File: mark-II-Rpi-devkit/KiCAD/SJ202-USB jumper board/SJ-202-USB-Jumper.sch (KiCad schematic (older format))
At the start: 3 parts, among them J1 USB_A, J2 USB3150-30-130-A, J3 Conn_01x05

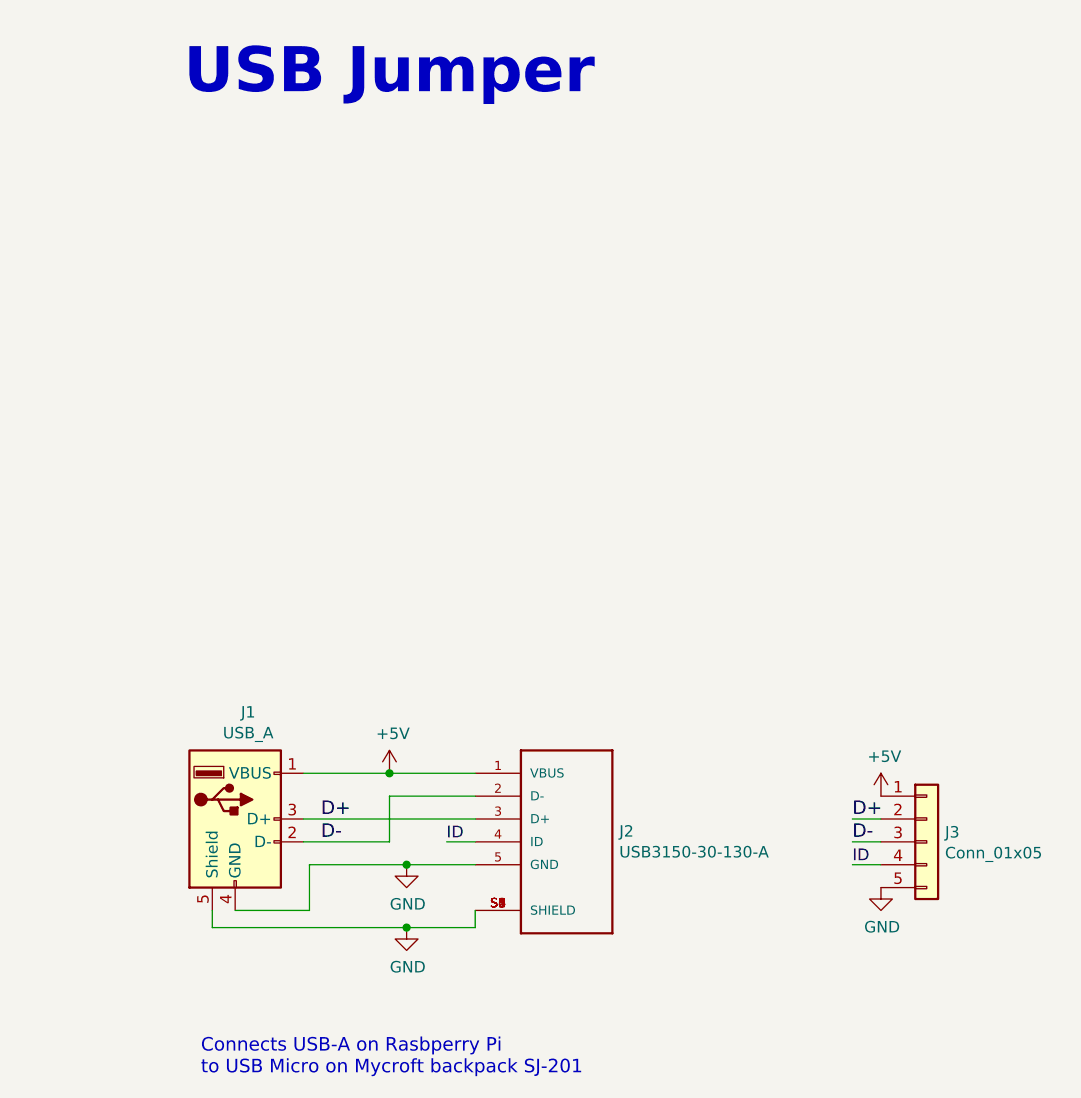
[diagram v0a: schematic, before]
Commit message: SJ201 - Removed CM108b soundcard, added in I2S to Line out, ATTin402. Moved holes in layout. SJ202 - extened length to plug into USB2.0 port
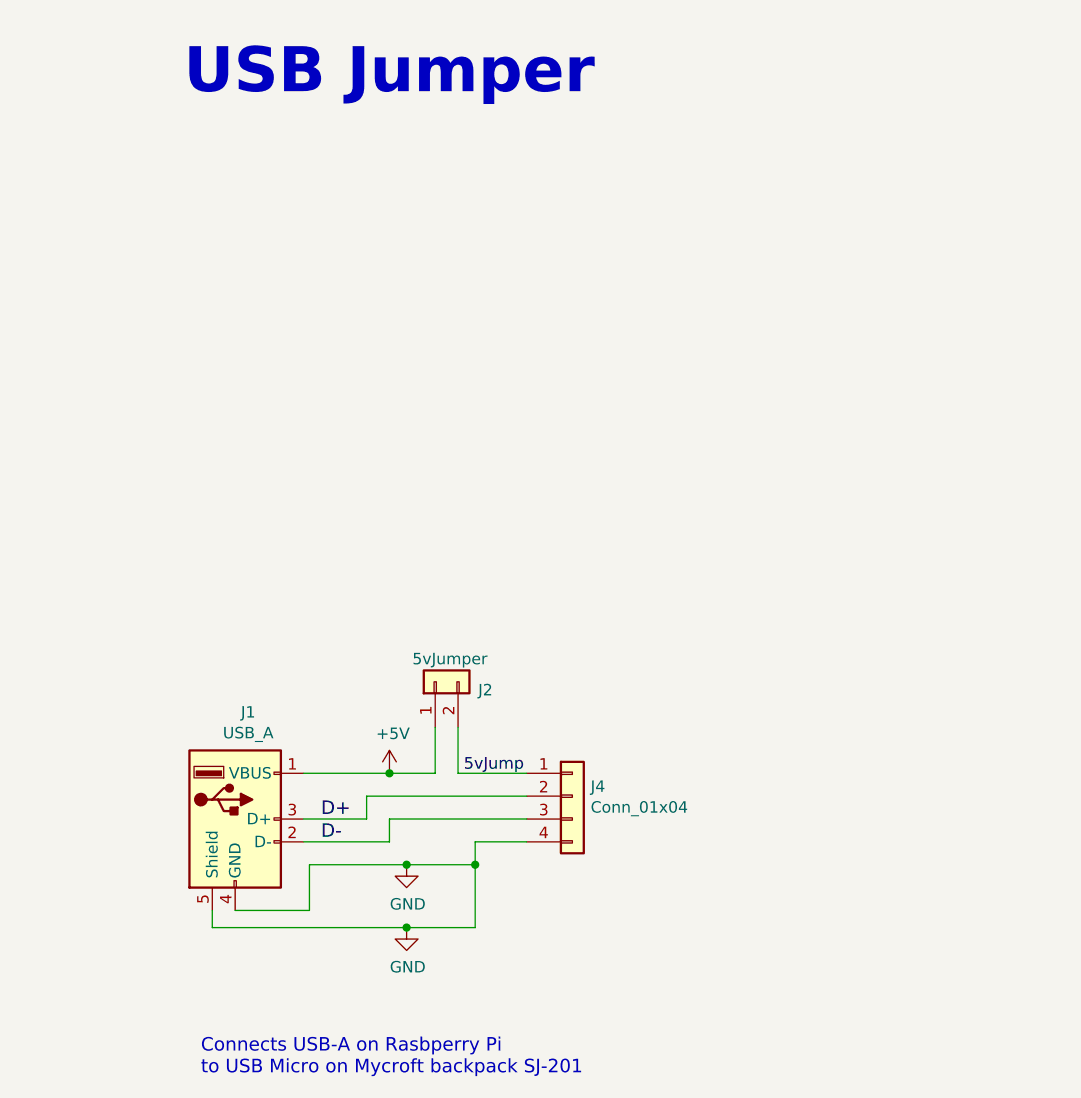
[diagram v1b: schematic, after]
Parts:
- removed J2: USB3150-30-130-A, GCT_USB3150-30-130-A, symbol USB3150-30-130-A:USB3150-30-130-A
- removed J3: Conn_01x05, Connector_PinHeader_2.54mm:PinHeader_1x05_P2.54mm_Vertical, symbol Connector_Generic:Conn_01x05
- added J2: 5vJumper, Jumper:SolderJumper-2_P1.3mm_Open_TrianglePad1.0x1.5mm, symbol Connector_Generic:Conn_01x02
- added J4: Conn_01x04, Connector_PinHeader_2.54mm:PinHeader_1x04_P2.54mm_Vertical, symbol Connector_Generic:Conn_01x04
- J1: Link (none) -> https://www.digikey.com/product-detail/en/0480372200/WM3983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; MPN (none) -> 0480372200
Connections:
- net +5V: now also J2.1 (Pin_1)
- net D+: now also J4.2 (Pin_2)
- net D-: now also J4.3 (Pin_3)
- net GND: now also J4.4 (Pin_4)
- new net 5vJump: J2.2 (Pin_2), J4.1 (Pin_1)
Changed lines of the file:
@@
 Sheet 1 1
 Title "SJ-202-USB-Jumper"
-Date "2020-09-04"
-Rev "01"
+Date "2020-09-27"
+Rev "02"
 Comp "Mycroft AI"
 Comment1 "SJ-202-01"
@@
 Comment4 ""
 $EndDescr
-$Comp
-L USB3150-30-130-A:USB3150-30-130-A J2
-U 1 1 5F5281B3
-P 5600 4175
-F 0 "J2" H 5830 4221 50  0000 L CNN
-F 1 "USB3150-30-130-A" H 5830 4130 50  0000 L CNN
-F 2 "GCT_USB3150-30-130-A" H 5600 4175 50  0001 L BNN
-F 3 "https://gct.co/files/drawings/usb3150.pdf" H 5600 4175 50  0001 L BNN
-F 4 "7.23mm" H 5600 4175 50  0001 L BNN "Field4"
-F 5 "A2" H 5600 4175 50  0001 L BNN "Field5"
-F 6 "GCT" H 5600 4175 50  0001 L BNN "Field6"
-F 7 "2073-USB3150-30-130-ACT-ND" H 5600 4175 50  0001 C CNN "Digikey"
-	1    5600 4175
-	1    0    0    -1
-$EndComp
 $Comp
 L Connector:USB_A J1
@@
 F 3 "https://www.digikey.com/product-detail/en/0480372200/WM3983CT-ND/2421836" H 4300 4025 50  0001 C CNN
 F 4 "WM3983CT-ND" H 4150 4075 50  0001 C CNN "Digikey"
+F 5 "0480372200" H 4150 4075 50  0001 C CNN "MPN"
+F 6 "https://www.digikey.com/product-detail/en/0480372200/WM3983CT-ND/2421836" H 4150 4075 50  0001 C CNN "Link"
 	1    4150 4075
 	1    0    0    -1
 $EndComp
-Wire Wire Line
-	5200 3875 4825 3875
-Wire Wire Line
-	4450 4075 5200 4075
-Wire Wire Line
-	5200 3975 4825 3975
-Wire Wire Line
-	4825 3975 4825 4175
 Wire Wire Line
 	4825 4175 4450 4175
@@
 Wire Wire Line
 	4050 4475 4050 4550
-Wire Wire Line
-	5200 4550 5200 4475
 $Comp
 L power:GND #PWR0101
@@
 	1    0    0    -1
 $EndComp
-Connection ~ 4825 3875
 Wire Wire Line
 	4825 3875 4450 3875
@@
 Text Notes 4000 5200 0    59   ~ 0
 Connects USB-A on Rasbperry Pi\nto USB Micro on Mycroft backpack SJ-201
-$Comp
-L Connector_Generic:Conn_01x05 J3
-U 1 1 5F52F406
-P 7175 4175
-F 0 "J3" H 7255 4217 50  0000 L CNN
-F 1 "Conn_01x05" H 7255 4126 50  0000 L CNN
-F 2 "Connector_PinHeader_2.54mm:PinHeader_1x05_P2.54mm_Vertical" H 7175 4175 50  0001 C CNN
-F 3 "~" H 7175 4175 50  0001 C CNN
-	1    7175 4175
-	1    0    0    -1
-$EndComp
 Wire Wire Line
 	4475 4475 4150 4475
@@
 Wire Wire Line
 	4900 4275 4475 4275
-$Comp
-L power:GND #PWR0104
-U 1 1 5F5305F9
-P 6975 4375
-F 0 "#PWR0104" H 6975 4125 50  0001 C CNN
-F 1 "GND" H 6980 4202 50  0000 C CNN
-F 2 "" H 6975 4375 50  0001 C CNN
-F 3 "" H 6975 4375 50  0001 C CNN
-	1    6975 4375
-	1    0    0    -1
-$EndComp
 Text Label 4525 4175 0    59   ~ 0
 D-
 Text Label 4525 4075 0    59   ~ 0
 D+
-Text Label 6850 4075 0    59   ~ 0
-D+
-Text Label 6850 4175 0    59   ~ 0
-D-
 $Comp
-L power:+5V #PWR0105
-U 1 1 5F530B0F
-P 6975 3975
-F 0 "#PWR0105" H 6975 3825 50  0001 C CNN
-F 1 "+5V" H 6990 4148 50  0000 C CNN
-F 2 "" H 6975 3975 50  0001 C CNN
-F 3 "" H 6975 3975 50  0001 C CNN
-	1    6975 3975
+L Connector_Generic:Conn_01x04 J4
+U 1 1 5F58F2C6
+P 5625 3975
+F 0 "J4" H 5705 4017 50  0000 L CNN
+F 1 "Conn_01x04" H 5705 3926 50  0000 L CNN
+F 2 "Connector_PinHeader_2.54mm:PinHeader_1x04_P2.54mm_Vertical" H 5625 3975 50  0001 C CNN
+F 3 "~" H 5625 3975 50  0001 C CNN
+F 4 "C124378" H 5625 3975 50  0001 C CNN "MPN"
+F 5 "C124378" H 5625 3975 50  0001 C CNN "LCSC"
+F 6 "https://lcsc.com/product-detail/Pin-Header-Female-Header_Ckmtw-Shenzhen-Cankemeng-C124378_C124378.html" H 5625 3975 50  0001 C CNN "Link"
+	1    5625 3975
 	1    0    0    -1
 $EndComp
+$Comp
+L Connector_Generic:Conn_01x02 J2
+U 1 1 5F596E74
+P 5025 3475
+F 0 "J2" V 4989 3287 50  0000 R CNN
+F 1 "5vJumper" V 5125 3575 50  0000 R CNN
+F 2 "Jumper:SolderJumper-2_P1.3mm_Open_TrianglePad1.0x1.5mm" H 5025 3475 50  0001 C CNN
+F 3 "~" H 5025 3475 50  0001 C CNN
+F 4 "DNP" H 5025 3475 50  0001 C CNN "MPN"
+	1    5025 3475
+	0    -1   -1   0
+$EndComp
 Wire Wire Line
-	6975 4075 6850 4075
+	5025 3675 5025 3875
 Wire Wire Line
-	6975 4175 6850 4175
+	5025 3875 4825 3875
+Connection ~ 4825 3875
 Wire Wire Line
-	5075 4175 5200 4175
-Text Label 5075 4175 0    51   ~ 0
-ID
-Text Label 6850 4275 0    51   ~ 0
-ID
+	5125 3675 5125 3875
+Connection ~ 5200 4275
 Wire Wire Line
-	6975 4275 6850 4275
+	5200 4275 5200 4550
+Wire Wire Line
+	5200 4175 5200 4275
+Wire Wire Line
+	4825 4075 4825 4175
+Wire Wire Line
+	4725 3975 4725 4075
+Wire Wire Line
+	4725 4075 4450 4075
+Text Label 5150 3875 0    51   ~ 0
+5vJump
+Wire Wire Line
+	5125 3875 5425 3875
+Wire Wire Line
+	4725 3975 5425 3975
+Wire Wire Line
+	4825 4075 5425 4075
+Wire Wire Line
+	5200 4175 5425 4175
 $EndSCHEMATC

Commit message: SJ-201 v3, sent to PCB Fab. Removed USB Hub, add in I2S to Line Out
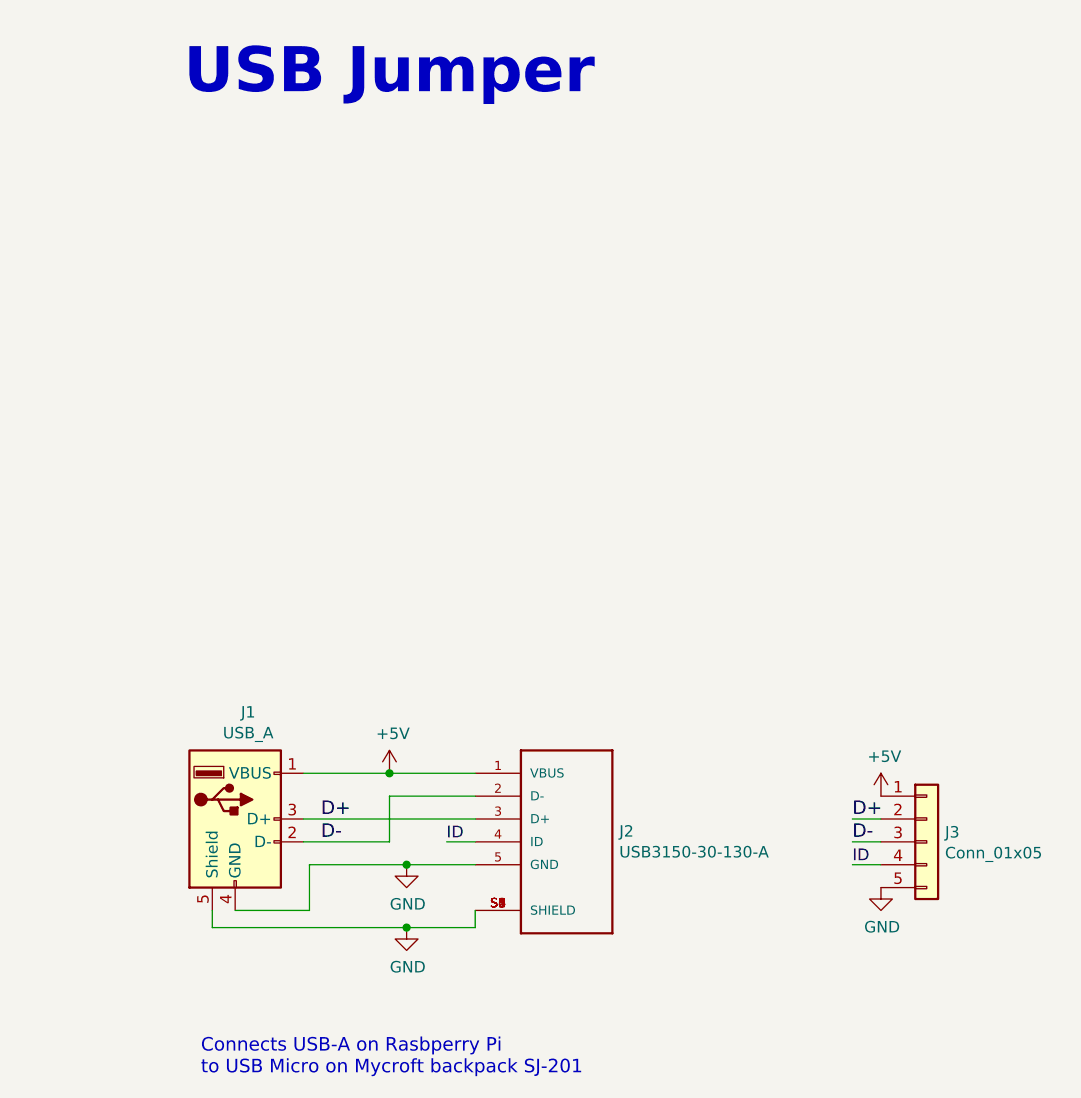
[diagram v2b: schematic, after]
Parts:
- removed J2: 5vJumper, Jumper:SolderJumper-2_P1.3mm_Open_TrianglePad1.0x1.5mm, symbol Connector_Generic:Conn_01x02
- removed J4: Conn_01x04, Connector_PinHeader_2.54mm:PinHeader_1x04_P2.54mm_Vertical, symbol Connector_Generic:Conn_01x04
- added J2: USB3150-30-130-A, GCT_USB3150-30-130-A, symbol USB3150-30-130-A:USB3150-30-130-A
- added J3: Conn_01x05, Connector_PinHeader_2.54mm:PinHeader_1x05_P2.54mm_Vertical, symbol Connector_Generic:Conn_01x05
- J1: Link https://www.digikey.com/product-detail/en/0480372200/WM3983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 -> (none); MPN 0480372200 -> (none)
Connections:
- net +5V: now also J2.1 (VBUS), J3.1 (Pin_1)
- net D+: now also J2.3 (D+), J3.2 (Pin_2)
- net D-: now also J2.2 (D-), J3.3 (Pin_3)
- net GND: now also J2.5 (GND), J2.S1 (SHIELD), J2.S2 (SHIELD), J2.S3 (SHIELD), J2.S4 (SHIELD), J2.S5 (SHIELD), J2.S6 (SHIELD), J3.5 (Pin_5)
- new net ID: J2.4 (ID), J3.4 (Pin_4)
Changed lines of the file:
@@
 Sheet 1 1
 Title "SJ-202-USB-Jumper"
-Date "2020-09-27"
-Rev "02"
+Date "2020-09-04"
+Rev "01"
 Comp "Mycroft AI"
 Comment1 "SJ-202-01"
@@
 Comment4 ""
 $EndDescr
+$Comp
+L USB3150-30-130-A:USB3150-30-130-A J2
+U 1 1 5F5281B3
+P 5600 4175
+F 0 "J2" H 5830 4221 50  0000 L CNN
+F 1 "USB3150-30-130-A" H 5830 4130 50  0000 L CNN
+F 2 "GCT_USB3150-30-130-A" H 5600 4175 50  0001 L BNN
+F 3 "https://gct.co/files/drawings/usb3150.pdf" H 5600 4175 50  0001 L BNN
+F 4 "7.23mm" H 5600 4175 50  0001 L BNN "Field4"
+F 5 "A2" H 5600 4175 50  0001 L BNN "Field5"
+F 6 "GCT" H 5600 4175 50  0001 L BNN "Field6"
+F 7 "2073-USB3150-30-130-ACT-ND" H 5600 4175 50  0001 C CNN "Digikey"
+	1    5600 4175
+	1    0    0    -1
+$EndComp
 $Comp
 L Connector:USB_A J1
@@
 F 3 "https://www.digikey.com/product-detail/en/0480372200/WM3983CT-ND/2421836" H 4300 4025 50  0001 C CNN
 F 4 "WM3983CT-ND" H 4150 4075 50  0001 C CNN "Digikey"
-F 5 "0480372200" H 4150 4075 50  0001 C CNN "MPN"
-F 6 "https://www.digikey.com/product-detail/en/0480372200/WM3983CT-ND/2421836" H 4150 4075 50  0001 C CNN "Link"
 	1    4150 4075
 	1    0    0    -1
 $EndComp
+Wire Wire Line
+	5200 3875 4825 3875
+Wire Wire Line
+	4450 4075 5200 4075
+Wire Wire Line
+	5200 3975 4825 3975
+Wire Wire Line
+	4825 3975 4825 4175
 Wire Wire Line
 	4825 4175 4450 4175
@@
 Wire Wire Line
 	4050 4475 4050 4550
+Wire Wire Line
+	5200 4550 5200 4475
 $Comp
 L power:GND #PWR0101
@@
 	1    0    0    -1
 $EndComp
+Connection ~ 4825 3875
 Wire Wire Line
 	4825 3875 4450 3875
@@
 Text Notes 4000 5200 0    59   ~ 0
 Connects USB-A on Rasbperry Pi\nto USB Micro on Mycroft backpack SJ-201
+$Comp
+L Connector_Generic:Conn_01x05 J3
+U 1 1 5F52F406
+P 7175 4175
+F 0 "J3" H 7255 4217 50  0000 L CNN
+F 1 "Conn_01x05" H 7255 4126 50  0000 L CNN
+F 2 "Connector_PinHeader_2.54mm:PinHeader_1x05_P2.54mm_Vertical" H 7175 4175 50  0001 C CNN
+F 3 "~" H 7175 4175 50  0001 C CNN
+	1    7175 4175
+	1    0    0    -1
+$EndComp
 Wire Wire Line
 	4475 4475 4150 4475
@@
 Wire Wire Line
 	4900 4275 4475 4275
+$Comp
+L power:GND #PWR0104
+U 1 1 5F5305F9
+P 6975 4375
+F 0 "#PWR0104" H 6975 4125 50  0001 C CNN
+F 1 "GND" H 6980 4202 50  0000 C CNN
+F 2 "" H 6975 4375 50  0001 C CNN
+F 3 "" H 6975 4375 50  0001 C CNN
+	1    6975 4375
+	1    0    0    -1
+$EndComp
 Text Label 4525 4175 0    59   ~ 0
 D-
 Text Label 4525 4075 0    59   ~ 0
 D+
+Text Label 6850 4075 0    59   ~ 0
+D+
+Text Label 6850 4175 0    59   ~ 0
+D-
 $Comp
-L Connector_Generic:Conn_01x04 J4
-U 1 1 5F58F2C6
-P 5625 3975
-F 0 "J4" H 5705 4017 50  0000 L CNN
-F 1 "Conn_01x04" H 5705 3926 50  0000 L CNN
-F 2 "Connector_PinHeader_2.54mm:PinHeader_1x04_P2.54mm_Vertical" H 5625 3975 50  0001 C CNN
-F 3 "~" H 5625 3975 50  0001 C CNN
-F 4 "C124378" H 5625 3975 50  0001 C CNN "MPN"
-F 5 "C124378" H 5625 3975 50  0001 C CNN "LCSC"
-F 6 "https://lcsc.com/product-detail/Pin-Header-Female-Header_Ckmtw-Shenzhen-Cankemeng-C124378_C124378.html" H 5625 3975 50  0001 C CNN "Link"
-	1    5625 3975
+L power:+5V #PWR0105
+U 1 1 5F530B0F
+P 6975 3975
+F 0 "#PWR0105" H 6975 3825 50  0001 C CNN
+F 1 "+5V" H 6990 4148 50  0000 C CNN
+F 2 "" H 6975 3975 50  0001 C CNN
+F 3 "" H 6975 3975 50  0001 C CNN
+	1    6975 3975
 	1    0    0    -1
 $EndComp
-$Comp
-L Connector_Generic:Conn_01x02 J2
-U 1 1 5F596E74
-P 5025 3475
-F 0 "J2" V 4989 3287 50  0000 R CNN
-F 1 "5vJumper" V 5125 3575 50  0000 R CNN
-F 2 "Jumper:SolderJumper-2_P1.3mm_Open_TrianglePad1.0x1.5mm" H 5025 3475 50  0001 C CNN
-F 3 "~" H 5025 3475 50  0001 C CNN
-F 4 "DNP" H 5025 3475 50  0001 C CNN "MPN"
-	1    5025 3475
-	0    -1   -1   0
-$EndComp
 Wire Wire Line
-	5025 3675 5025 3875
+	6975 4075 6850 4075
 Wire Wire Line
-	5025 3875 4825 3875
-Connection ~ 4825 3875
+	6975 4175 6850 4175
 Wire Wire Line
-	5125 3675 5125 3875
-Connection ~ 5200 4275
+	5075 4175 5200 4175
+Text Label 5075 4175 0    51   ~ 0
+ID
+Text Label 6850 4275 0    51   ~ 0
+ID
 Wire Wire Line
-	5200 4275 5200 4550
-Wire Wire Line
-	5200 4175 5200 4275
-Wire Wire Line
-	4825 4075 4825 4175
-Wire Wire Line
-	4725 3975 4725 4075
-Wire Wire Line
-	4725 4075 4450 4075
-Text Label 5150 3875 0    51   ~ 0
-5vJump
-Wire Wire Line
-	5125 3875 5425 3875
-Wire Wire Line
-	4725 3975 5425 3975
-Wire Wire Line
-	4825 4075 5425 4075
-Wire Wire Line
-	5200 4175 5425 4175
+	6975 4275 6850 4275
 $EndSCHEMATC
